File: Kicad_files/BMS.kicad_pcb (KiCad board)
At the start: 2 copper layers, 29.2 x 27.8 mm, 22 parts, among them J1 USB_B_Mini, Q1 SQJ418EP-T1_GE3, Q2 SQJ418EP-T1_GE3, Q3 SQJ418EP-T1_GE3, U1 BQ297xy, U2 MCP73831-2-OT

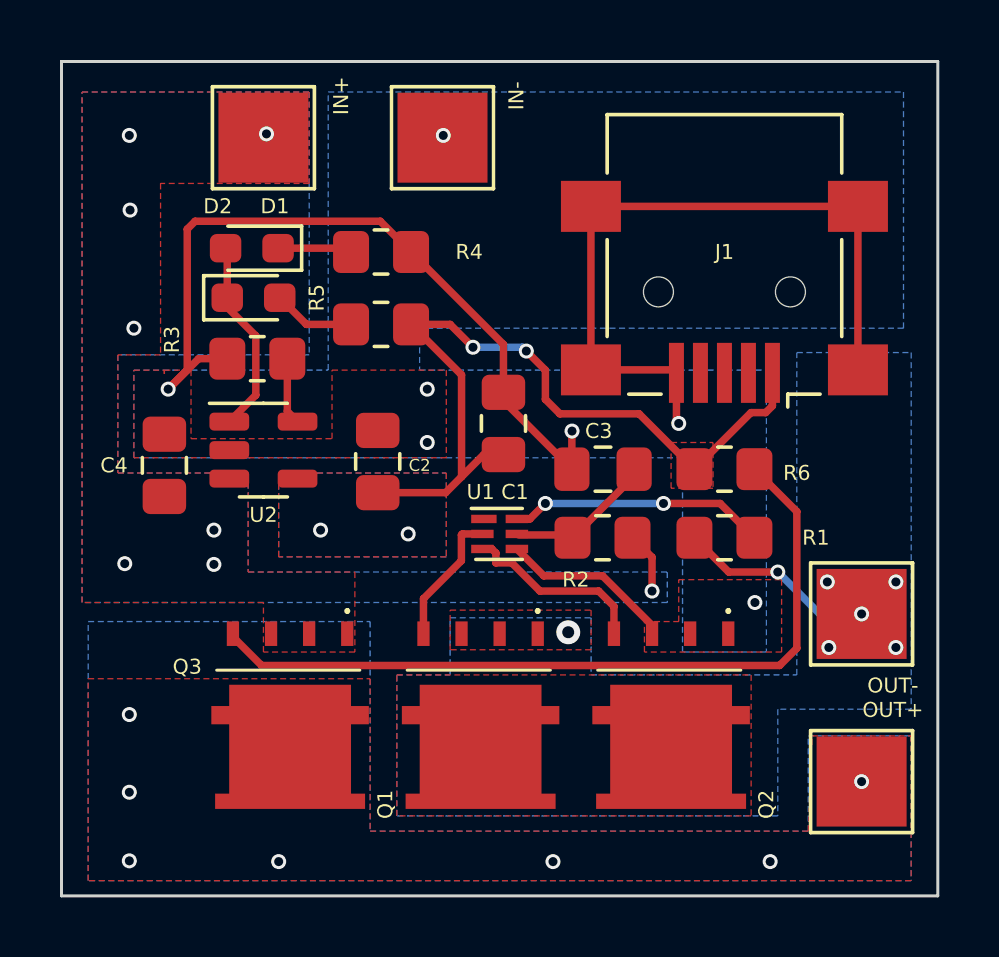
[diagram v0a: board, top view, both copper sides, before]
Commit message: new kicad files to reflect v1.1 changes
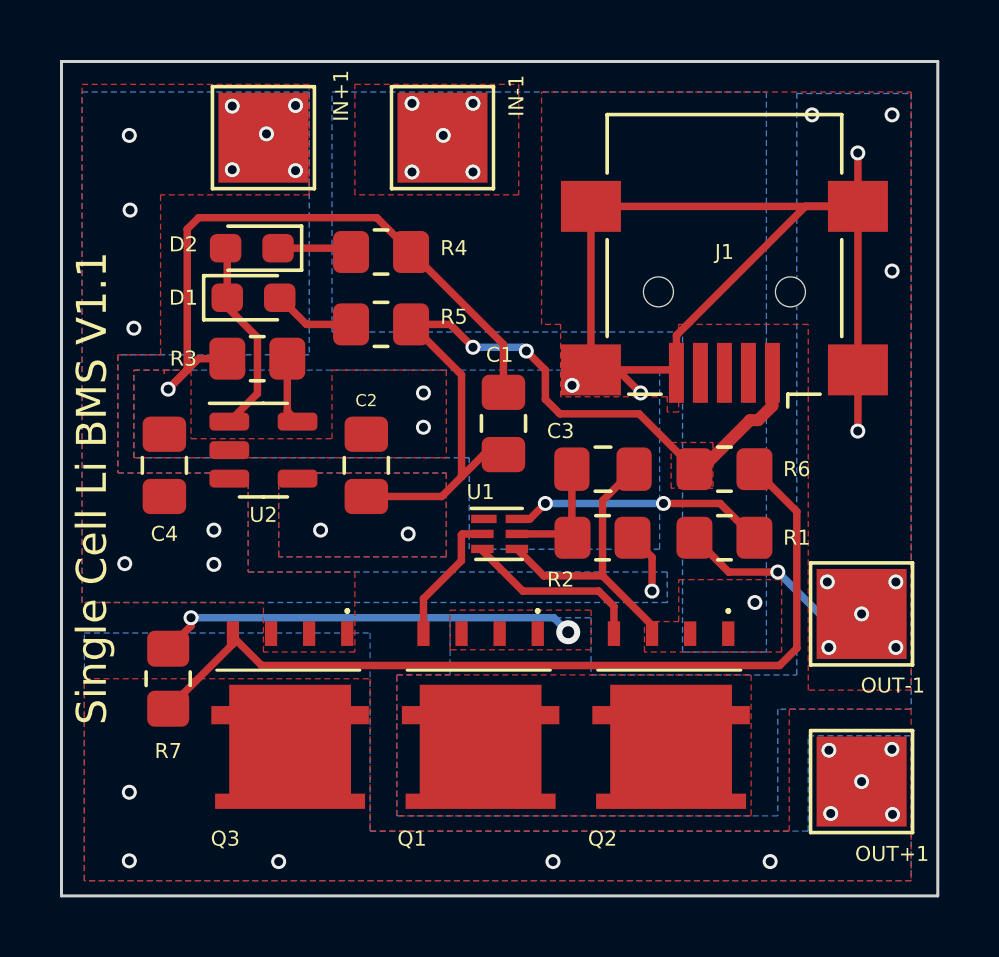
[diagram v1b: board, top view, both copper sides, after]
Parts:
- added R7: 10000, Resistor_SMD:R_0805_2012Metric_Pad1.20x1.40mm_HandSolder, F.Cu at (112.4, 62.4)
- Q1, Q2: value SQJ418EP-T1_GE3 -> NMOS
- Q3: value SQJ418EP-T1_GE3 -> PMOS
- moved C2 0.40 mm to (119.0, 55.2)
- turned C3 to 0 degrees
- renumbered IN+ to IN+1, IN- to IN-1, OUT+ to OUT+1, OUT- to OUT-1
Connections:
- C1 pad 2: V_BAT_NEG -> VP_BATT_NEG
- C2 pad 2: V_BAT_NEG -> VP_BATT_NEG
- C4 pad 2: V_BAT_NEG -> VP_BATT_NEG
- J1 pad 5: V_BAT_NEG -> VP_BATT_NEG
- J1 pad 6: V_BAT_NEG -> VP_BATT_NEG
- R3 pad 2: V_BAT_NEG -> VP_BATT_NEG
- R4 pad 2: V_BAT_NEG -> VP_BATT_NEG
- U2 pad 2: V_BAT_NEG -> VP_BATT_NEG
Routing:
- net VP_BATT_NEG: track 6.62 -> 81.1 mm, vias 7 -> 18
- net V_BAT_NEG: track 57.1 -> 10.3 mm, vias 7 -> 6
- net Net-(Q3-Pad4): track 26.1 -> 29.5 mm
- net Net-(C3-Pad1): track 5.22 -> 4.20 mm
- net +5V: track 27.1 -> 27.8 mm
- net V_BAT_POS: vias 8 -> 12
- net VP_BATT_POS: vias 7 -> 10
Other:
- board text added: "Single Cell Li BMS V1.1"
